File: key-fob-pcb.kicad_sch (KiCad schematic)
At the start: 1 part

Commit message: changed button to active high and added a few DNP buttons
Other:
- sheet User IO ports: added VCC; removed none
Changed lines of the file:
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@@
+    (stroke (width 0) (type default))
+  )
+  (wire (pts (xy 142.24 93.98) (xy 147.32 93.98))
     (stroke (width 0) (type default))
   )
@@
   (label "START_STOP" (at 184.15 46.99 0) (fields_autoplaced)
     (effects (font (size 1.27 1.27)) (justify left bottom))
+  )
+  (label "VCC" (at 142.24 93.98 180) (fields_autoplaced)
+    (effects (font (size 1.27 1.27)) (justify right bottom))
   )
   (label "EN" (at 184.15 67.31 0) (fields_autoplaced)
@@
       (effects (font (size 1.27 1.27)) (justify right))
     )
+    (pin "VCC" input (at 147.32 93.98 180)
+      (effects (font (size 1.27 1.27)) (justify left))
+    )
     (instances

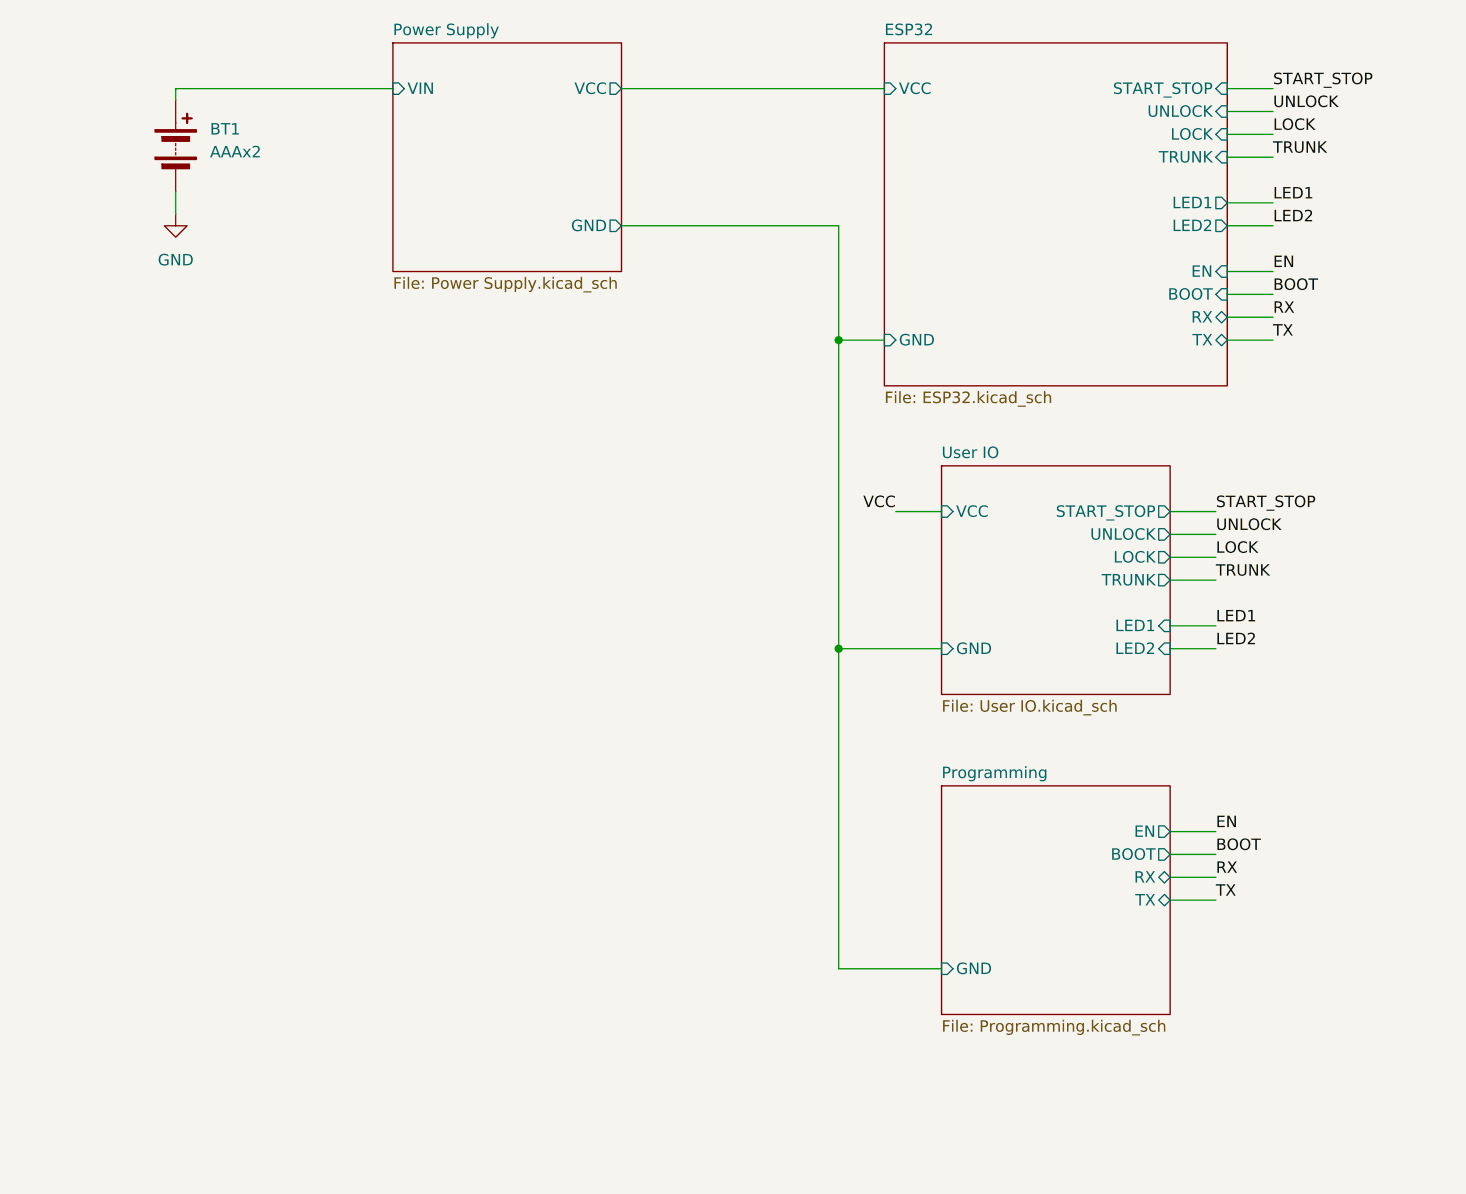
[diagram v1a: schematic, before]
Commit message: add ADC circuit, a few more DNP components, and assigned footprints
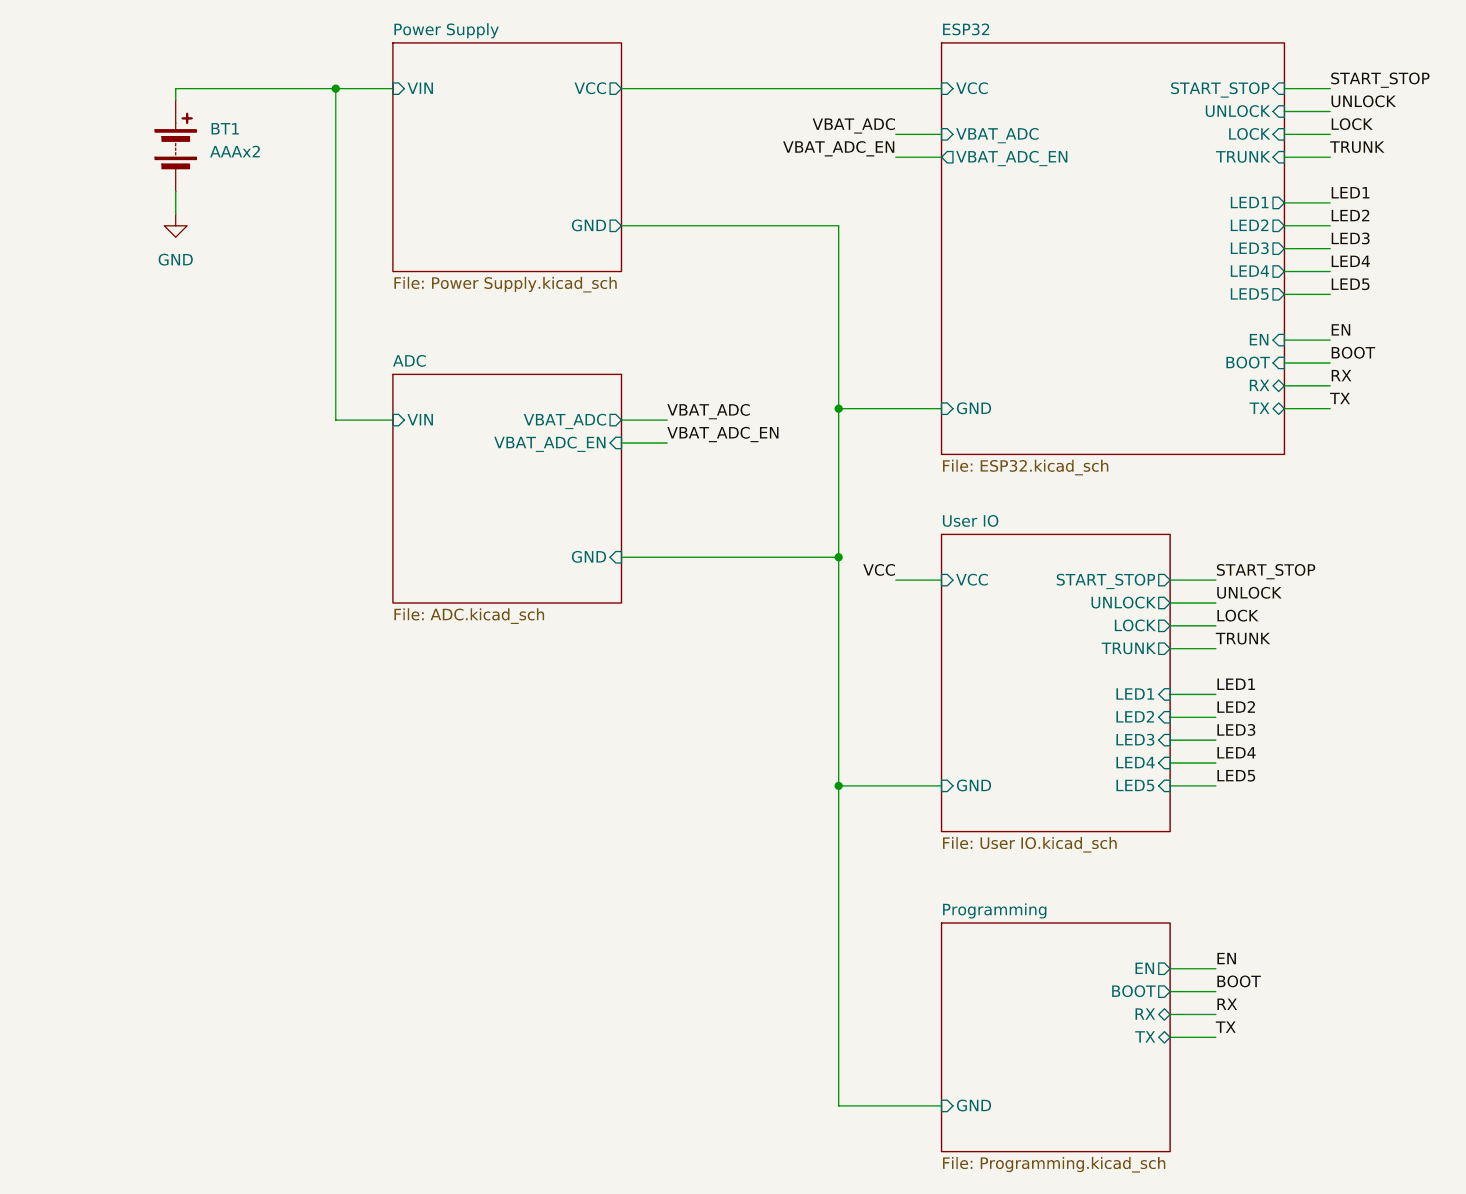
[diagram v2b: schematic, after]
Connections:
- net Power Supply/VIN renamed ADC/VIN
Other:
- added sheet ADC (ADC.kicad_sch)
- sheet ESP32 ports: added LED3, LED4, LED5, VBAT_ADC, VBAT_ADC_EN; removed none
- sheet User IO ports: added LED3, LED4, LED5; removed none

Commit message: create libraries folder for sharing external libs
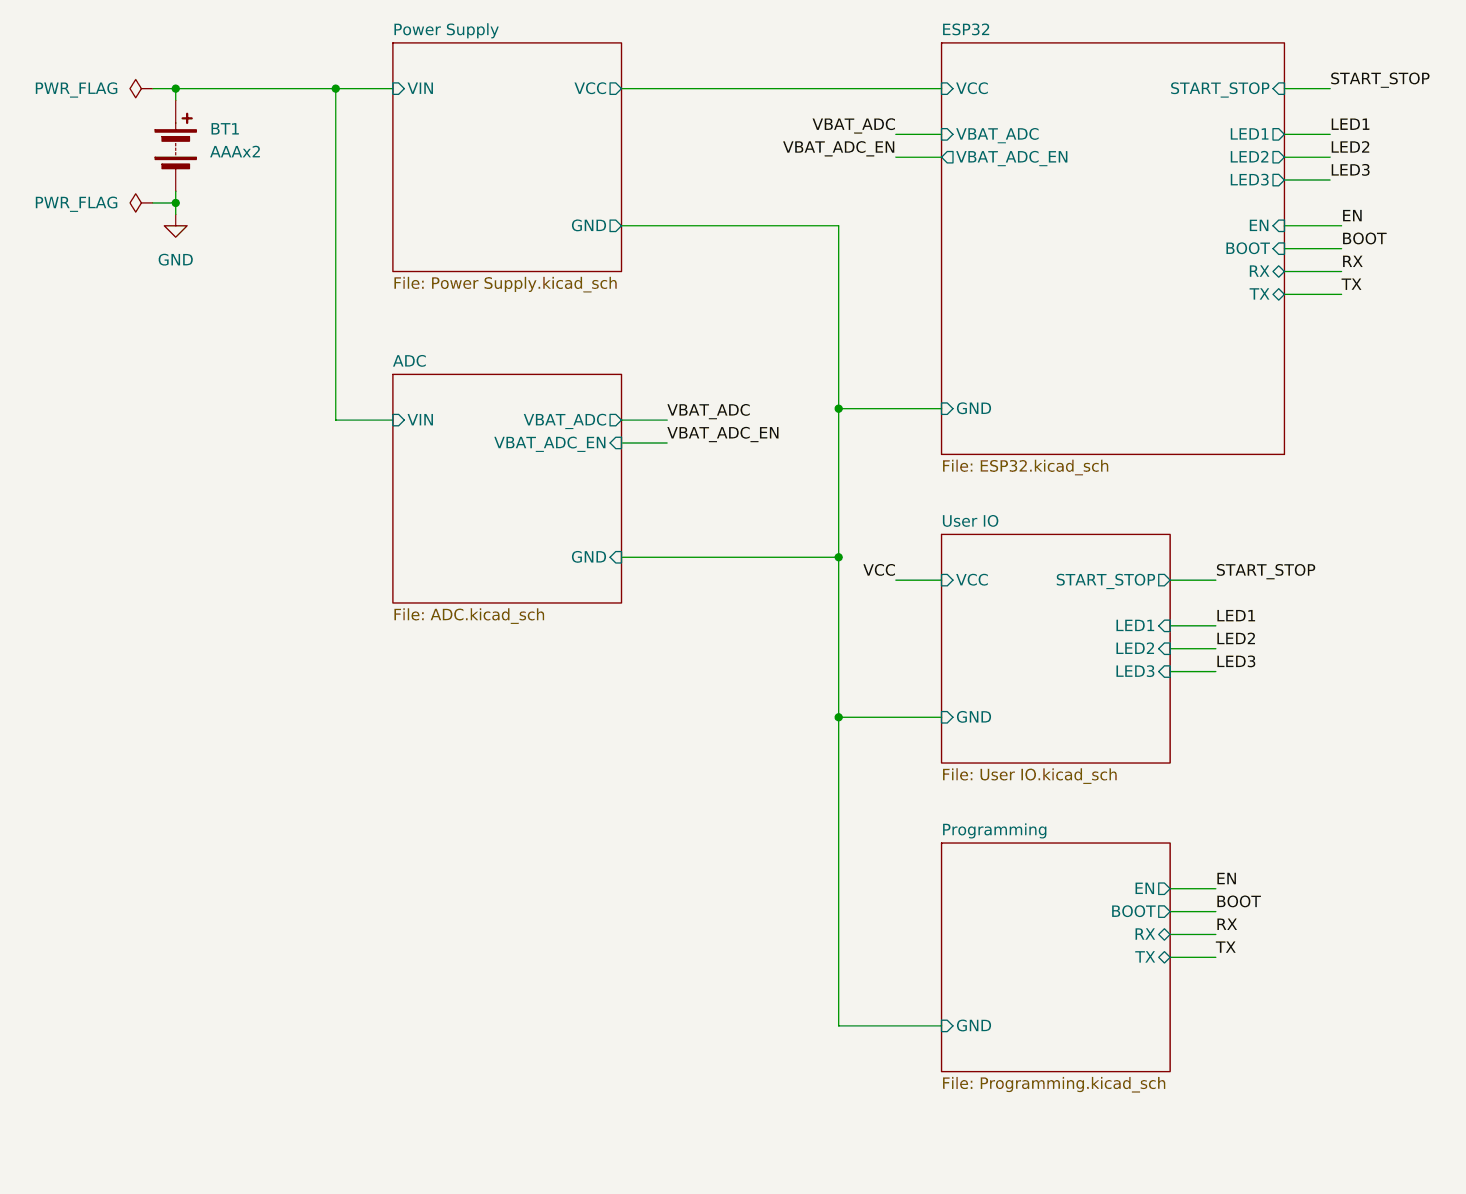
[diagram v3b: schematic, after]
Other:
- sheet ESP32 ports: added none; removed LED4, LED5, LOCK, TRUNK, UNLOCK
- sheet User IO ports: added none; removed LED4, LED5, LOCK, TRUNK, UNLOCK

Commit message: inital layout of components complete
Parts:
- removed BT1: AAAx2, symbol Device:Battery
- added BT1: 2468, 2468:BAT_2468, symbol 2468:2468
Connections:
- net ADC/VIN: now also BT1.P
- net GND: now also BT1.N
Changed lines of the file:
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@@
   (junction (at 62.23 46.99) (diameter 0) (color 0 0 0 0)
   )
-  (junction (at 62.23 59.69) (diameter 0) (color 0 0 0 0)
+  (junction (at 62.23 64.77) (diameter 0) (color 0 0 0 0)
   )
   (junction (at 80.01 46.99) (diameter 0) (color 0 0 0 0)
@@
     (stroke (width 0) (type default))
   )
-  (wire (pts (xy 59.69 59.69) (xy 62.23 59.69))
+  (wire (pts (xy 111.76 46.99) (xy 116.84 46.99))
+    (stroke (width 0) (type default))
+  )
+  (wire (pts (xy 59.69 64.77) (xy 62.23 64.77))
     (stroke (width 0) (type default))
   )
@@
     (stroke (width 0) (type default))
   )
-  (wire (pts (xy 111.76 46.99) (xy 147.32 46.99))
+  (wire (pts (xy 142.24 46.99) (xy 147.32 46.99))
     (stroke (width 0) (type default))
   )
@@
     (stroke (width 0) (type default))
   )
-  (wire (pts (xy 62.23 58.42) (xy 62.23 59.69))
+  (wire (pts (xy 62.23 63.5) (xy 62.23 64.77))
     (stroke (width 0) (type default))
   )
@@
     (stroke (width 0) (type default))
   )
-  (wire (pts (xy 62.23 59.69) (xy 62.23 60.96))
+  (wire (pts (xy 62.23 64.77) (xy 62.23 66.04))
     (stroke (width 0) (type default))
   )
@@
     (effects (font (size 1.27 1.27)) (justify left bottom))
   )
+  (label "VCC" (at 142.24 46.99 180) (fields_autoplaced)
+    (effects (font (size 1.27 1.27)) (justify right bottom))
+  )
   (label "LED3" (at 177.8 111.76 0) (fields_autoplaced)
     (effects (font (size 1.27 1.27)) (justify left bottom))
   )
+  (label "VCC" (at 116.84 46.99 0) (fields_autoplaced)
+    (effects (font (size 1.27 1.27)) (justify left bottom))
+  )
   (label "LED2" (at 190.5 54.61 0) (fields_autoplaced)
     (effects (font (size 1.27 1.27)) (justify left bottom))
@@
   (label "VBAT_ADC_EN" (at 142.24 54.61 180) (fields_autoplaced)
     (effects (font (size 1.27 1.27)) (justify right bottom))
+  )
+  (symbol (lib_id "2468:2468") (at 62.23 55.88 270) (unit 1)
+    (in_bom yes) (on_board yes) (dnp no) (fields_autoplaced)
+    (property "Reference" "BT1" (at 66.04 53.975 90)
+      (effects (font (size 1.27 1.27)) (justify left))
+    )
+    (property "Value" "2468" (at 66.04 56.515 90)
+      (effects (font (size 1.27 1.27)) (justify left))
+    )
+    (property "Footprint" "2468:BAT_2468" (at 62.23 55.88 0)
+      (effects (font (size 1.27 1.27)) (justify bottom) hide)
+    )
+    (property "Datasheet" "" (at 62.23 55.88 0)
+      (effects (font (size 1.27 1.27)) hide)
+    )
+    (property "PARTREV" "D" (at 62.23 55.88 0)
+      (effects (font (size 1.27 1.27)) (justify bottom) hide)
+    )
+    (property "STANDARD" "Manufacturer Recommendations" (at 62.23 55.88 0)
+      (effects (font (size 1.27 1.27)) (justify bottom) hide)
+    )
+    (property "SNAPEDA_PN" "2468" (at 62.23 55.88 0)
+      (effects (font (size 1.27 1.27)) (justify bottom) hide)
+    )
+    (property "MAXIMUM_PACKAGE_HEIGHT" "13.25" (at 62.23 55.88 0)
+      (effects (font (size 1.27 1.27)) (justify bottom) hide)
+    )
+    (property "MANUFACTURER" "Keystone" (at 62.23 55.88 0)
+      (effects (font (size 1.27 1.27)) (justify bottom) hide)
+    )
+    (pin "N")
+    (pin "P")
+    (instances
+      (project "key-fob-pcb"
+        (path "/b002c3bf-fc58-4993-80f7-7914d3aa1ac9"
+          (reference "BT1") (unit 1)
+        )
+      )
+    )
   )
   (symbol (lib_id "power:PWR_FLAG") (at 59.69 46.99 90) (unit 1)
@@
     )
   )
-  (symbol (lib_id "power:PWR_FLAG") (at 59.69 59.69 90) (unit 1)
-    (in_bom yes) (on_board yes) (dnp no) (fields_autoplaced)
-    (property "Reference" "#FLG02" (at 57.785 59.69 0)
-      (effects (font (size 1.27 1.27)) hide)
-    )
-    (property "Value" "PWR_FLAG" (at 55.88 59.69 90)
-      (effects (font (size 1.27 1.27)) (justify left))
-    )
-    (property "Footprint" "" (at 59.69 59.69 0)
-      (effects (font (size 1.27 1.27)) hide)
-    )
-    (property "Datasheet" "~" (at 59.69 59.69 0)
+  (symbol (lib_id "power:PWR_FLAG") (at 59.69 64.77 90) (unit 1)
+    (in_bom yes) (on_board yes) (dnp no) (fields_autoplaced)
+    (property "Reference" "#FLG02" (at 57.785 64.77 0)
+      (effects (font (size 1.27 1.27)) hide)
+    )
+    (property "Value" "PWR_FLAG" (at 55.88 64.77 90)
+      (effects (font (size 1.27 1.27)) (justify left))
+    )
+    (property "Footprint" "" (at 59.69 64.77 0)
+      (effects (font (size 1.27 1.27)) hide)
+    )
+    (property "Datasheet" "~" (at 59.69 64.77 0)
       (effects (font (size 1.27 1.27)) hide)
     )
@@
     )
   )
-  (symbol (lib_id "Device:Battery") (at 62.23 53.34 0) (unit 1)
-    (in_bom yes) (on_board yes) (dnp no) (fields_autoplaced)
-    (property "Reference" "BT1" (at 66.04 51.4985 0)
-      (effects (font (size 1.27 1.27)) (justify left))
-    )
-    (property "Value" "AAAx2" (at 66.04 54.0385 0)
-      (effects (font (size 1.27 1.27)) (justify left))
-    )
-    (property "Footprint" "" (at 62.23 51.816 90)
-      (effects (font (size 1.27 1.27)) hide)
-    )
-    (property "Datasheet" "~" (at 62.23 51.816 90)
-      (effects (font (size 1.27 1.27)) hide)
-    )
-    (pin "1")
-    (pin "2")
-    (instances
-      (project "key-fob-pcb"
-        (path "/b002c3bf-fc58-4993-80f7-7914d3aa1ac9"
-          (reference "BT1") (unit 1)
-        )
-      )
-    )
-  )
-  (symbol (lib_id "power:GND") (at 62.23 60.96 0) (unit 1)
-    (in_bom yes) (on_board yes) (dnp no) (fields_autoplaced)
-    (property "Reference" "#PWR01" (at 62.23 67.31 0)
-      (effects (font (size 1.27 1.27)) hide)
-    )
-    (property "Value" "GND" (at 62.23 66.04 0)
+  (symbol (lib_id "power:GND") (at 62.23 66.04 0) (unit 1)
+    (in_bom yes) (on_board yes) (dnp no) (fields_autoplaced)
+    (property "Reference" "#PWR01" (at 62.23 72.39 0)
+      (effects (font (size 1.27 1.27)) hide)
+    )
+    (property "Value" "GND" (at 62.23 71.12 0)
       (effects (font (size 1.27 1.27)))
     )
-    (property "Footprint" "" (at 62.23 60.96 0)
-      (effects (font (size 1.27 1.27)) hide)
-    )
-    (property "Datasheet" "" (at 62.23 60.96 0)
-      (effects (font (size 1.27 1.27)) hide)
-    )
+    (property "Footprint" "" (at 62.23 66.04 0)
+      (effects (font (size 1.27 1.27)) hide)
+    )
+    (property "Datasheet" "" (at 62.23 66.04 0)
+      (effects (font (size 1.27 1.27)) hide)
+    )
